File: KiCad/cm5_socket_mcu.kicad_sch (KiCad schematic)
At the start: 4 parts, among them IC1 AZ1117CH2-3.3TRG1

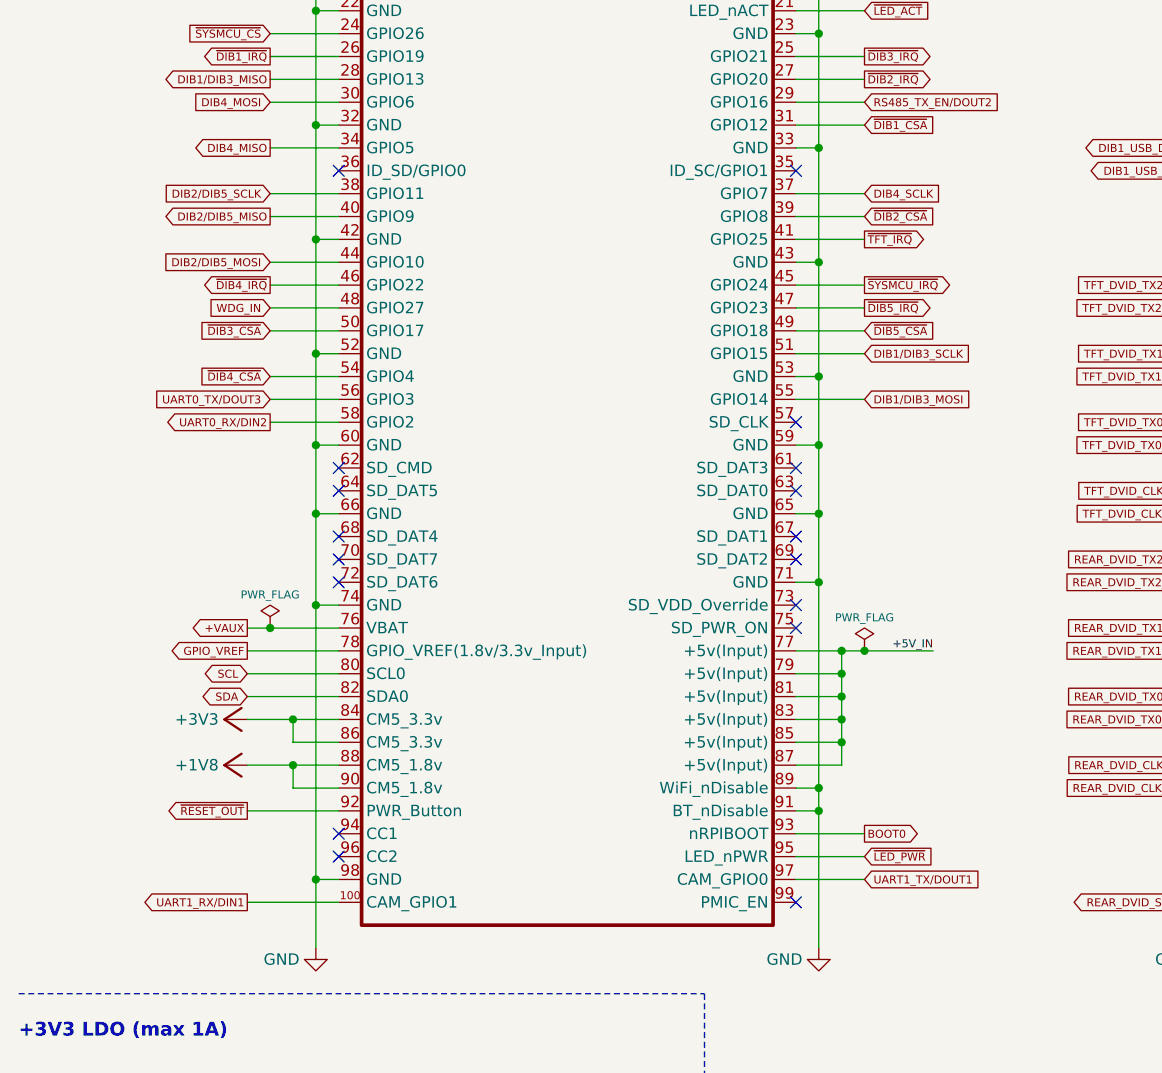
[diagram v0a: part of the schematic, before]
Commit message: DIN3 pin assigned
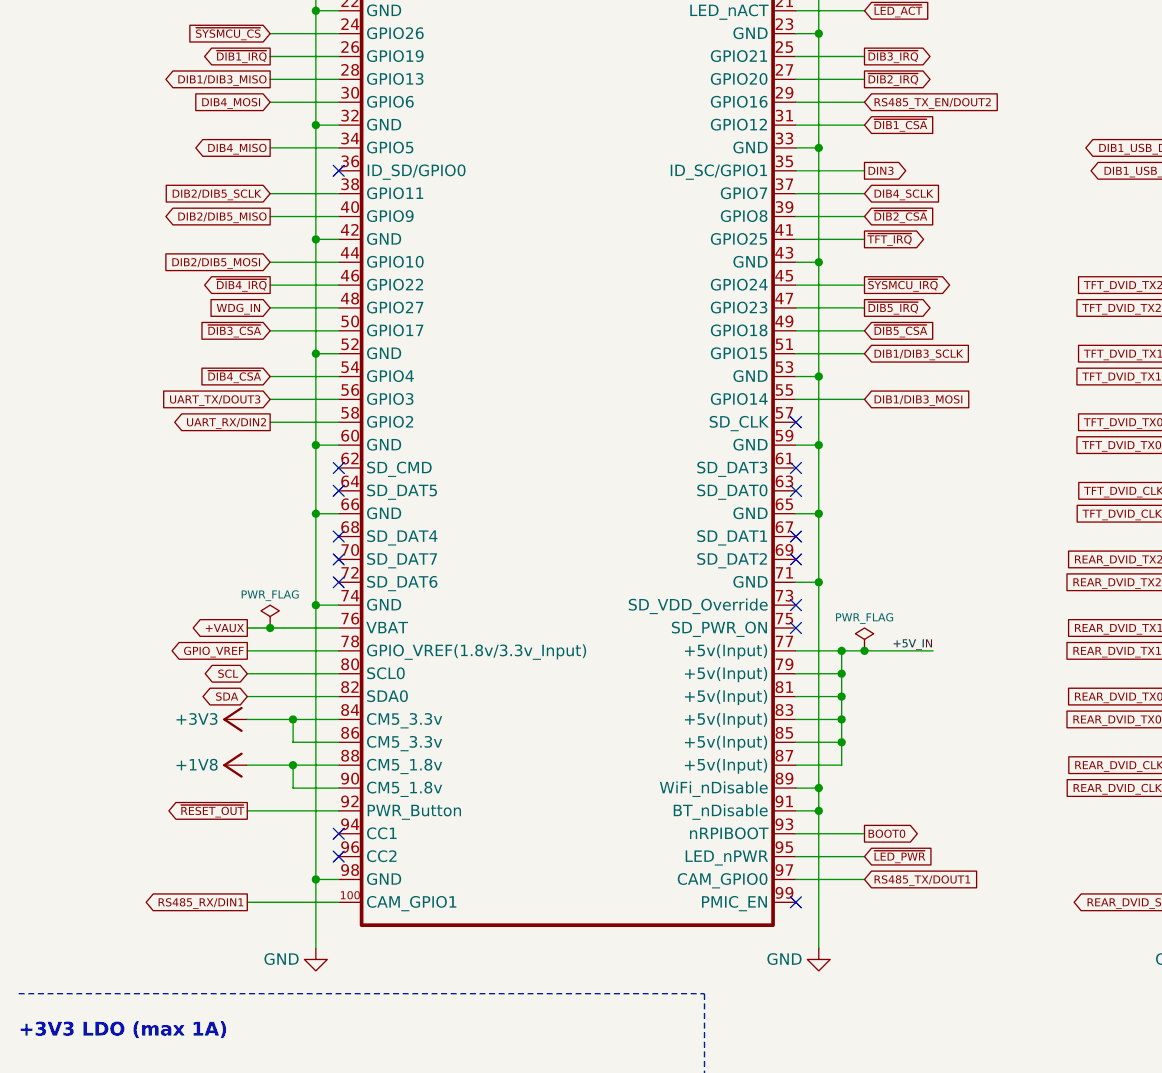
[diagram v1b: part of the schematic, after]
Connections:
- net DIN3: now reaches SoM1.35 (ID_SC/GPIO1)
- net UART0_RX/DIN2 renamed UART_RX/DIN2
- net UART0_TX/DOUT3 renamed UART_TX/DOUT3
- net UART1_RX/DIN1 renamed RS485_RX/DIN1
- net UART1_TX/DOUT1 renamed RS485_TX/DOUT1
- no-connect marks 71 -> 70
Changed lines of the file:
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@@
 	(title_block
 		(title "${project_name}")
-		(date "2025-11-03")
+		(date "2025-11-23")
 		(rev "${project_version}")
 		(company "${project_creator}")

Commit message: ETH clk fixed, digital I/O naming updated
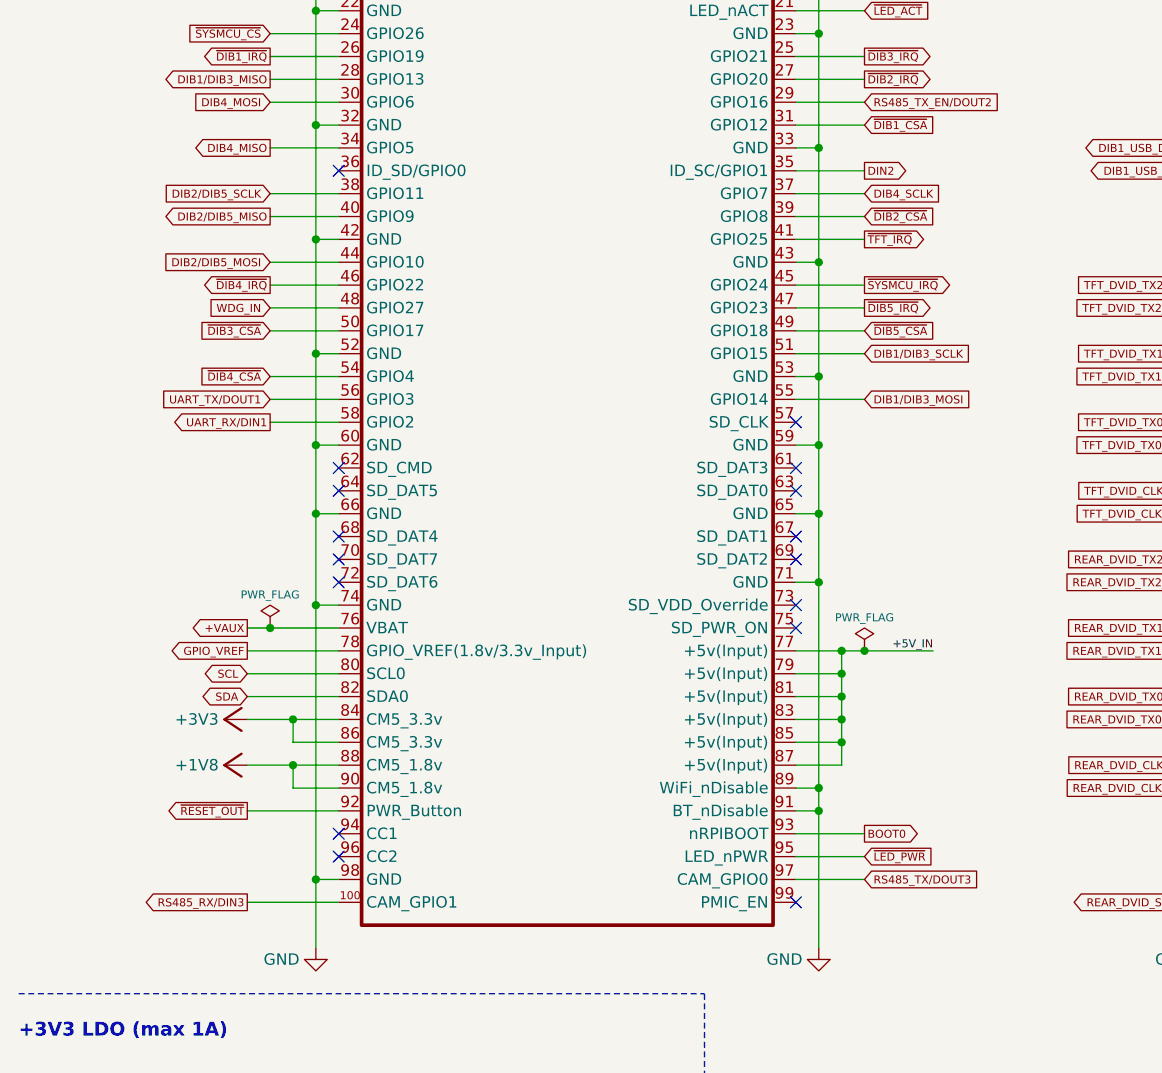
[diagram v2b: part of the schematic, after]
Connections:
- net DIN3 renamed DIN2
- net RS485_RX/DIN1 renamed RS485_RX/DIN3
- net RS485_TX/DOUT1 renamed RS485_TX/DOUT3
- net UART_RX/DIN2 renamed UART_RX/DIN1
- net UART_TX/DOUT3 renamed UART_TX/DOUT1
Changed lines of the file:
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@@
 	(title_block
 		(title "${project_name}")
-		(date "2025-11-23")
+		(date "2025-11-24")
 		(rev "${project_version}")
 		(company "${project_creator}")

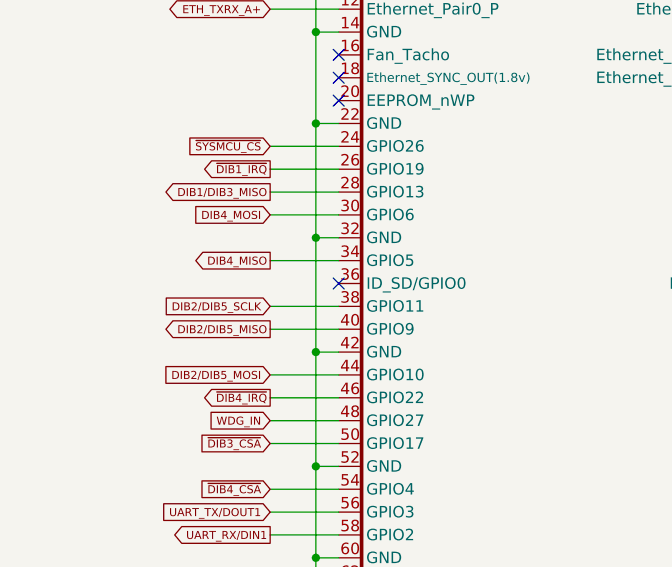
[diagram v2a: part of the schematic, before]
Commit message: RTC input added
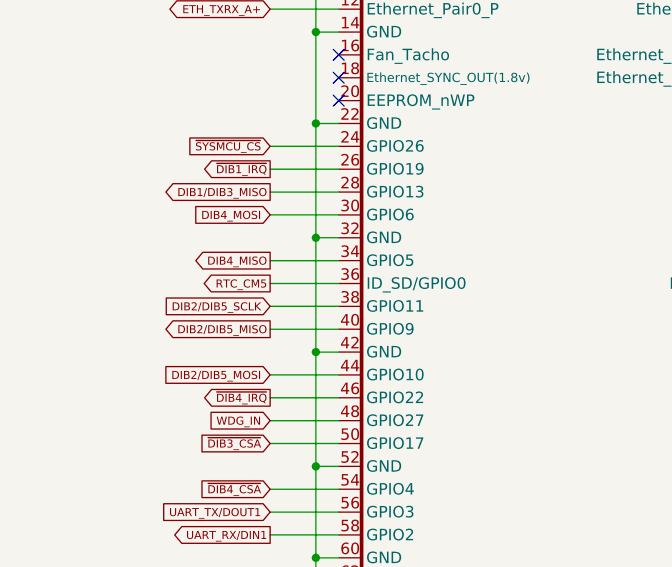
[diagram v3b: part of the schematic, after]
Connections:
- net RTC_CM5: now reaches SoM1.36 (ID_SD/GPIO0)
- no-connect marks 70 -> 69
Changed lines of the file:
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@@
 	(title_block
 		(title "${project_name}")
-		(date "2025-11-24")
+		(date "2025-11-28")
 		(rev "${project_version}")
 		(company "${project_creator}")

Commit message: #1, #2, #3
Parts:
- added JP2: ~, PCM_EEZ_SMD:JP2 shorted (0603), symbol PCM_EEZ_unsorted:JP2 shorted
- SoM1: DigiKey 26-DF40HC(3.0)-100DS-0.4V(51)CT-ND -> H11614CT-ND; LCSC C424649 -> C531031; Mouser 798-DF40HC30100DS451 -> 798-DF40C100DP0.4V51; TME - -> DF40C-100DP-04V-51
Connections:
- net GND: now also SoM1.SH, JP2.2
- net at SoM1.111 (VBUS_EN_(3.3v)): now also JP2.1
- net WDG_IN renamed DIB_OE_SYNC
- no-connect marks 69 -> 68

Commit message: #4
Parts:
- renumbered JP2 to JP1
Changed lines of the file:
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@@
 	(title_block
 		(title "${project_name}")
-		(date "2025-12-19")
+		(date "2025-12-24")
 		(rev "${project_version}")
 		(company "${project_creator}")
@@
 		(on_board yes)
 		(dnp no)
-		(property "Reference" "#PWR06"
+		(property "Reference" "#PWR07"
 			(at 104.14 161.29 0)
 			(effects
@@
 			(project "BB3plus CM5 STM32H7 module"
 				(path "/1a4f0aea-3a69-423f-8790-3103cd0321c4/c2910023-6066-4877-a406-045757318a99"
-					(reference "#PWR06")
+					(reference "#PWR07")
 					(unit 1)
 				)
@@
 		(on_board yes)
 		(dnp no)
-		(property "Reference" "#PWR08"
+		(property "Reference" "#PWR09"
 			(at 208.28 161.29 0)
 			(effects
@@
 			(project "BB3plus CM5 STM32H7 module"
 				(path "/1a4f0aea-3a69-423f-8790-3103cd0321c4/c2910023-6066-4877-a406-045757318a99"
-					(reference "#PWR08")
+					(reference "#PWR09")
 					(unit 1)
 				)
@@
 		(on_board yes)
 		(dnp no)
-		(property "Reference" "JP2"
+		(property "Reference" "JP1"
 			(at 208.915 38.1 0)
 			(effects
@@
 			(project ""
 				(path "/1a4f0aea-3a69-423f-8790-3103cd0321c4/c2910023-6066-4877-a406-045757318a99"
-					(reference "JP2")
+					(reference "JP1")
 					(unit 1)
 				)
@@
 		(on_board yes)
 		(dnp no)
-		(property "Reference" "#PWR07"
+		(property "Reference" "#PWR08"
 			(at 147.32 161.29 0)
 			(effects
@@
 			(project "BB3plus CM5 STM32H7 module"
 				(path "/1a4f0aea-3a69-423f-8790-3103cd0321c4/c2910023-6066-4877-a406-045757318a99"
-					(reference "#PWR07")
+					(reference "#PWR08")
 					(unit 1)
 				)
@@
 		(on_board yes)
 		(dnp no)
-		(property "Reference" "#PWR019"
+		(property "Reference" "#PWR06"
 			(at 76.2 161.29 0)
 			(effects
@@
 			(project "BB3plus CM5 STM32H7 module"
 				(path "/1a4f0aea-3a69-423f-8790-3103cd0321c4/c2910023-6066-4877-a406-045757318a99"
-					(reference "#PWR019")
+					(reference "#PWR06")
 					(unit 1)
 				)

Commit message: #7
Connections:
- net +5V_IN renamed +5V
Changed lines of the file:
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@@
 	(wire
 		(pts
-			(xy 109.22 121.92) (xy 116.84 121.92)
+			(xy 109.22 121.92) (xy 111.76 121.92)
 		)
 		(stroke
@@
 	(wire
 		(pts
+			(xy 27.94 175.26) (xy 30.48 175.26)
+		)
+		(stroke
+			(width 0)
+			(type default)
+		)
+	)
+	(wire
+		(pts
 			(xy 43.18 68.58) (xy 50.8 68.58)
 		)
@@
 	(wire
 		(pts
-			(xy 30.48 175.26) (xy 22.86 175.26)
-		)
-		(stroke
-			(width 0)
-			(type default)
-		)
-	)
-	(wire
-		(pts
 			(xy 147.32 71.12) (xy 149.86 71.12)
 		)
@@
 		)
 	)
-	(label "+5V_IN"
-		(at 116.84 121.92 180)
-		(effects
-			(font
-				(size 0.889 0.889)
-			)
-			(justify right bottom)
-		)
-	)
-	(label "+5V_IN"
-		(at 22.86 175.26 0)
-		(effects
-			(font
-				(size 0.889 0.889)
-			)
-			(justify left bottom)
-		)
-	)
 	(global_label "TFT_DVID_CLK_N"
 		(shape input)
@@
 	)
 	(symbol
+		(lib_id "PCM_EEZ_symbols:+5V")
+		(at 25.4 175.26 90)
+		(unit 1)
+		(exclude_from_sim no)
+		(in_bom yes)
+		(on_board yes)
+		(dnp no)
+		(property "Reference" "#+5V01"
+			(at 25.4 175.26 0)
+			(effects
+				(font
+					(size 1.27 1.27)
+				)
+				(hide yes)
+			)
+		)
+		(property "Value" "+5V"
+			(at 24.765 175.26 90)
+			(effects
+				(font
+					(size 1.27 1.27)
+				)
+				(justify left)
+			)
+		)
+		(property "Footprint" ""
+			(at 25.4 175.26 0)
+			(effects
+				(font
+					(size 1.27 1.27)
+				)
+				(hide yes)
+			)
+		)
+		(property "Datasheet" ""
+			(at 25.4 175.26 0)
+			(effects
+				(font
+					(size 1.27 1.27)
+				)
+				(hide yes)
+			)
+		)
+		(property "Description" ""
+			(at 25.4 175.26 0)
+			(effects
+				(font
+					(size 1.27 1.27)
+				)
+				(hide yes)
+			)
+		)
+		(pin "1"
+		)
+		(instances
+			(project ""
+				(path "/1a4f0aea-3a69-423f-8790-3103cd0321c4/c2910023-6066-4877-a406-045757318a99"
+					(reference "#+5V01")
+					(unit 1)
+				)
+			)
+		)
+	)
+	(symbol
 		(lib_id "power:PWR_FLAG")
 		(at 109.22 121.92 0)
@@
 					(unit 1)
 				)
+			)
+		)
+	)
+	(symbol
+		(lib_id "PCM_EEZ_symbols:+5V")
+		(at 114.3 121.92 270)
+		(mirror x)
+		(unit 1)
+		(exclude_from_sim no)
+		(in_bom yes)
+		(on_board yes)
+		(dnp no)
+		(property "Reference" "#+5V02"
+			(at 114.3 121.92 0)
+			(effects
+				(font
+					(size 1.27 1.27)
+				)
+				(hide yes)
+			)
+		)
+		(property "Value" "+5V"
+			(at 114.935 121.92 90)
+			(effects
+				(font
+					(size 1.27 1.27)
+				)
+				(justify left)
+			)
+		)
+		(property "Footprint" ""
+			(at 114.3 121.92 0)
+			(effects
+				(font
+					(size 1.27 1.27)
+				)
+				(hide yes)
+			)
+		)
+		(property "Datasheet" ""
+			(at 114.3 121.92 0)
+			(effects
+				(font
+					(size 1.27 1.27)
+				)
+				(hide yes)
+			)
+		)
+		(property "Description" ""
+			(at 114.3 121.92 0)
+			(effects
+				(font
+					(size 1.27 1.27)
+				)
+				(hide yes)
+			)
+		)
+		(pin "1"
+		)
+		(instances
+			(project "BB3plus CM5 STM32H7 module"
+				(path "/1a4f0aea-3a69-423f-8790-3103cd0321c4/c2910023-6066-4877-a406-045757318a99"
+					(reference "#+5V02")
+					(unit 1)
+				)

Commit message: #9
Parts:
- removed JP1: ~, PCM_EEZ_SMD:JP2 shorted (0603), symbol PCM_EEZ_unsorted:JP2 shorted
- added C3: 100n, PCM_EEZ_passives:C_0402_1005Metric, symbol PCM_EEZ_passives:C-EU
- added IC2: PI3USB102ZLEX, PCM_EEZ_SMD:TQFN-10, symbol PCM_EEZ_ICs:PI3USB102ZLEX
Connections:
- net +3V3: now also C3.2, IC2.9 (Vdd)
- net GND: now also C3.1, IC2.3 (GND), IC2.8 (~{OE})
- net MCU_USB_UP_TX+: now also IC2.1 (Y+); no longer SoM1.171 (USB3-1-TX_P)
- net MCU_USB_UP_TX-: now also IC2.2 (Y-); no longer SoM1.169 (USB3-1-TX_N)
- net MCU_USB_VBUS: now reaches SoM1.111 (VBUS_EN_(3.3v))
- net MCU_USB_ID: now reaches SoM1.101 (USB_OTG_ID)
- net USB2-: now reaches SoM1.103 (USB_N)
- net USB2-: now also IC2.4 (M-)
- net USB2+: now reaches SoM1.105 (USB_P)
- net USB2+: now also IC2.5 (M+)
- new net USB3_1+: IC2.7 (D+), SoM1.171 (USB3-1-TX_P)
- new net USB3_1-: IC2.6 (D-), SoM1.169 (USB3-1-TX_N)
- new net USB_FS_SEL: IC2.10 (S)
- no-connect marks 68 -> 65
